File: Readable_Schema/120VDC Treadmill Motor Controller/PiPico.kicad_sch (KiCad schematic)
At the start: 1 part

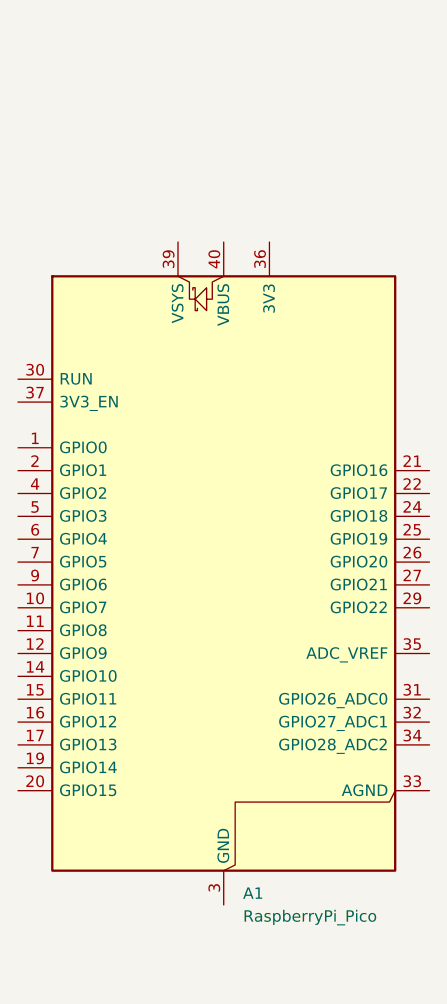
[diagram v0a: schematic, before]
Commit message: I cant for the life of me get the current sensing to actually properly scale with current, I treid 5 different sim models and right now the DA is the best but doesnt start showing anything till around 19amps which kind of defeats the purpose
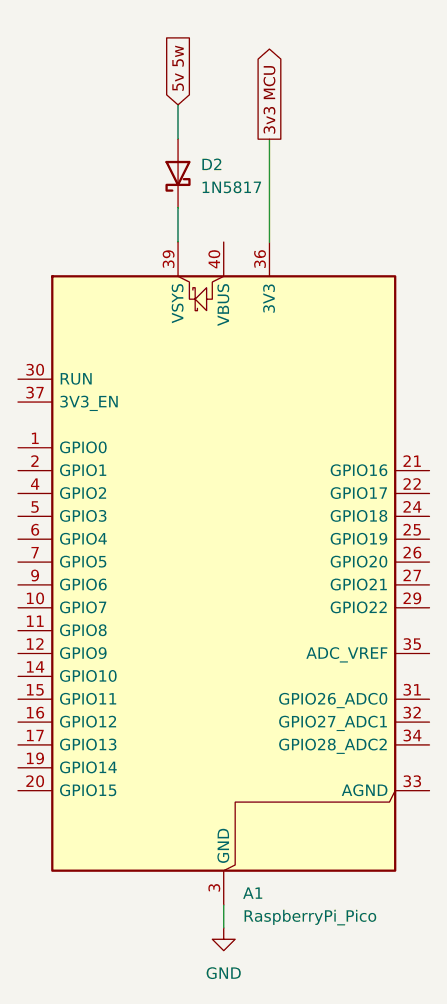
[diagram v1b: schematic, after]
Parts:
- added D2: 1N5817, Diode_THT:D_DO-41_SOD81_P10.16mm_Horizontal, symbol Diode:1N5817
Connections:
- net GND: now reaches A1.13 (GND), A1.18 (GND), A1.23 (GND), A1.28 (GND), A1.3 (GND), A1.38 (GND), A1.8 (GND)
- net 3v3 MCU: now reaches A1.36 (3V3)
- net at A1.39 (VSYS): now also D2.1 (K)
- new net 5v 5w: D2.2 (A)
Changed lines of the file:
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@@
 	(generator_version "9.0")
 	(paper "A4")
+	(wire
+		(pts
+			(xy 135.89 58.42) (xy 135.89 62.23)
+		)
+		(stroke
+			(width 0)
+			(type default)
+		)
+	)
+	(wire
+		(pts
+			(xy 135.89 46.99) (xy 135.89 50.8)
+		)
+		(stroke
+			(width 0)
+			(type default)
+		)
+	)
+	(wire
+		(pts
+			(xy 140.97 135.89) (xy 140.97 138.43)
+		)
+		(stroke
+			(width 0)
+			(type default)
+		)
+	)
+	(wire
+		(pts
+			(xy 146.05 50.8) (xy 146.05 62.23)
+		)
+		(stroke
+			(width 0)
+			(type default)
+		)
+	)
+	(global_label "5v 5w"
+		(shape input)
+		(at 135.89 46.99 90)
+		(fields_autoplaced yes)
+		(effects
+			(font
+				(size 1.27 1.27)
+			)
+			(justify left)
+		)
+		(property "Intersheetrefs" "${INTERSHEET_REFS}"
+			(at 135.89 38.3201 90)
+			(effects
+				(font
+					(size 1.27 1.27)
+				)
+				(justify left)
+				(hide yes)
+			)
+		)
+	)
+	(global_label "3v3 MCU"
+		(shape output)
+		(at 146.05 50.8 90)
+		(fields_autoplaced yes)
+		(effects
+			(font
+				(size 1.27 1.27)
+			)
+			(justify left)
+		)
+		(property "Intersheetrefs" "${INTERSHEET_REFS}"
+			(at 146.05 39.4087 90)
+			(effects
+				(font
+					(size 1.27 1.27)
+				)
+				(justify left)
+				(hide yes)
+			)
+		)
+	)
 	(symbol
 		(lib_id "MCU_Module:RaspberryPi_Pico")
@@
 					(unit 1)
 				)
+			)
+		)
+	)
+	(symbol
+		(lib_id "power:GND")
+		(at 140.97 138.43 0)
+		(unit 1)
+		(exclude_from_sim no)
+		(in_bom yes)
+		(on_board yes)
+		(dnp no)
+		(fields_autoplaced yes)
+		(property "Reference" "#PWR03"
+			(at 140.97 144.78 0)
+			(effects
+				(font
+					(size 1.27 1.27)
+				)
+				(hide yes)
+			)
+		)
+		(property "Value" "GND"
+			(at 140.97 143.51 0)
+			(effects
+				(font
+					(size 1.27 1.27)
+				)
+			)
+		)
+		(property "Footprint" ""
+			(at 140.97 138.43 0)
+			(effects
+				(font
+					(size 1.27 1.27)
+				)
+				(hide yes)
+			)
+		)
+		(property "Datasheet" ""
+			(at 140.97 138.43 0)
+			(effects
+				(font
+					(size 1.27 1.27)
+				)
+				(hide yes)
+			)
+		)
+		(property "Description" "Power symbol creates a global label with name \"GND\" , ground"
+			(at 140.97 138.43 0)
+			(effects
+				(font
+					(size 1.27 1.27)
+				)
+				(hide yes)
+			)
+		)
+		(pin "1"
+		)
+		(instances
+			(project ""
+				(path "/319bc5c0-2dd5-4df3-a34b-9170833ebccd/dc45a2ff-df18-49a4-81ff-80d10381c9e9"
+					(reference "#PWR03")
+					(unit 1)
+				)
+			)
+		)
+	)
+	(symbol
+		(lib_id "Diode:1N5817")
+		(at 135.89 54.61 90)
+		(unit 1)
+		(exclude_from_sim no)
+		(in_bom yes)
+		(on_board yes)
+		(dnp no)
+		(fields_autoplaced yes)
+		(property "Reference" "D2"
+			(at 138.43 53.6574 90)
+			(effects
+				(font
+					(size 1.27 1.27)
+				)
+				(justify right)
+			)
+		)
+		(property "Value" "1N5817"
+			(at 138.43 56.1974 90)
+			(effects
+				(font
+					(size 1.27 1.27)
+				)
+				(justify right)
+			)
+		)
+		(property "Footprint" "Diode_THT:D_DO-41_SOD81_P10.16mm_Horizontal"
+			(at 140.335 54.61 0)
+			(effects
+				(font
+					(size 1.27 1.27)
+				)
+				(hide yes)
+			)
+		)
+		(property "Datasheet" "http://www.vishay.com/docs/88525/1n5817.pdf"
+			(at 135.89 54.61 0)
+			(effects
+				(font
+					(size 1.27 1.27)
+				)
+				(hide yes)
+			)
+		)
+		(property "Description" "20V 1A Schottky Barrier Rectifier Diode, DO-41"
+			(at 135.89 54.61 0)
+			(effects
+				(font
+					(size 1.27 1.27)
+				)
+				(hide yes)
+			)
+		)
+		(pin "1"
+		)
+		(pin "2"
+		)
+		(instances
+			(project ""
+				(path "/319bc5c0-2dd5-4df3-a34b-9170833ebccd/dc45a2ff-df18-49a4-81ff-80d10381c9e9"
+					(reference "D2")
+					(unit 1)
+				)

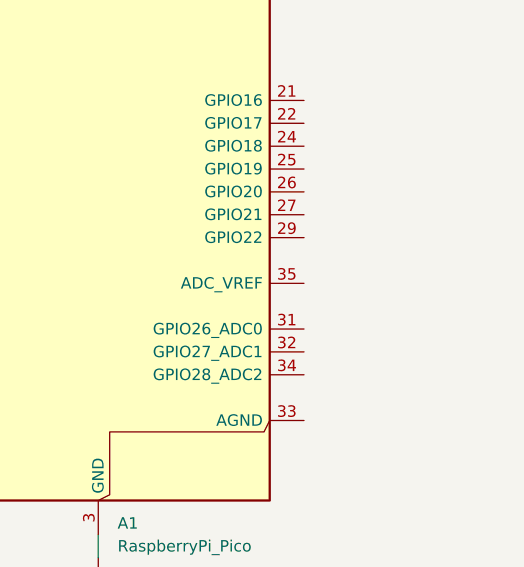
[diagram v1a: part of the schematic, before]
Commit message: Continuing to update footprints, did some follow up math on low pass filter for adc voltage coming out of current sense system
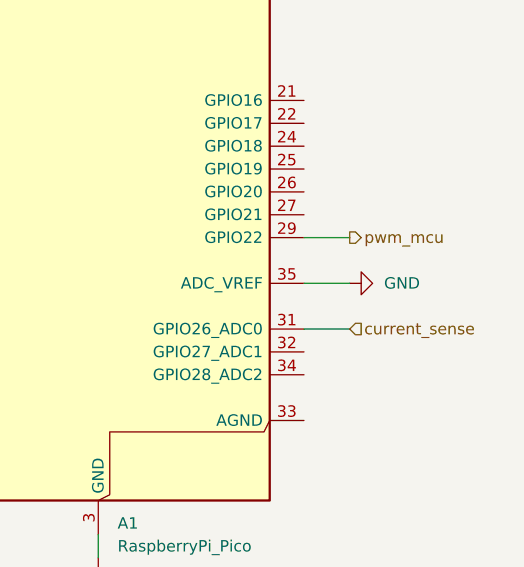
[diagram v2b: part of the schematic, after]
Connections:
- net GND: now also A1.35 (ADC_VREF)
- net pwm_mcu: now reaches A1.29 (GPIO22)
- net current_sense: now reaches A1.31 (GPIO26_ADC0)
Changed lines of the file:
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@@
+	(wire
+		(pts
+			(xy 163.83 107.95) (xy 168.91 107.95)
+		)
+		(stroke
+			(width 0)
+			(type default)
+		)
+	)
 	(wire
 		(pts
@@
 	(wire
 		(pts
+			(xy 163.83 102.87) (xy 168.91 102.87)
+		)
+		(stroke
+			(width 0)
+			(type default)
+		)
+	)
+	(wire
+		(pts
 			(xy 140.97 135.89) (xy 140.97 138.43)
 		)
@@
 		(pts
 			(xy 146.05 50.8) (xy 146.05 62.23)
+		)
+		(stroke
+			(width 0)
+			(type default)
+		)
+	)
+	(wire
+		(pts
+			(xy 163.83 113.03) (xy 168.91 113.03)
 		)
 		(stroke
@@
 				(hide yes)
 			)
+		)
+	)
+	(hierarchical_label "pwm_mcu"
+		(shape output)
+		(at 168.91 102.87 0)
+		(effects
+			(font
+				(size 1.27 1.27)
+			)
+			(justify left)
+		)
+	)
+	(hierarchical_label "current_sense"
+		(shape input)
+		(at 168.91 113.03 0)
+		(effects
+			(font
+				(size 1.27 1.27)
+			)
+			(justify left)
 		)
 	)
@@
 					(unit 1)
 				)
+			)
+		)
+	)
+	(symbol
+		(lib_id "power:GND")
+		(at 168.91 107.95 90)
+		(unit 1)
+		(exclude_from_sim no)
+		(in_bom yes)
+		(on_board yes)
+		(dnp no)
+		(fields_autoplaced yes)
+		(property "Reference" "#PWR020"
+			(at 175.26 107.95 0)
+			(effects
+				(font
+					(size 1.27 1.27)
+				)
+				(hide yes)
+			)
+		)
+		(property "Value" "GND"
+			(at 172.72 107.9499 90)
+			(effects
+				(font
+					(size 1.27 1.27)
+				)
+				(justify right)
+			)
+		)
+		(property "Footprint" ""
+			(at 168.91 107.95 0)
+			(effects
+				(font
+					(size 1.27 1.27)
+				)
+				(hide yes)
+			)
+		)
+		(property "Datasheet" ""
+			(at 168.91 107.95 0)
+			(effects
+				(font
+					(size 1.27 1.27)
+				)
+				(hide yes)
+			)
+		)
+		(property "Description" "Power symbol creates a global label with name \"GND\" , ground"
+			(at 168.91 107.95 0)
+			(effects
+				(font
+					(size 1.27 1.27)
+				)
+				(hide yes)
+			)
+		)
+		(pin "1"
+		)
+		(instances
+			(project "120VDC Treadmill Motor Controller"
+				(path "/319bc5c0-2dd5-4df3-a34b-9170833ebccd/dc45a2ff-df18-49a4-81ff-80d10381c9e9"
+					(reference "#PWR020")
+					(unit 1)
+				)

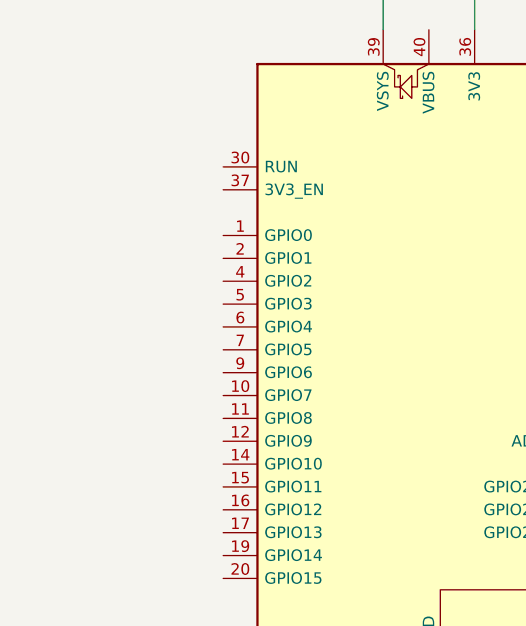
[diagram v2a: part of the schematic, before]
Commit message: continued to add footprints, we still need to add hall effect circuit and possible brake resistor subcircuit. We may also want to consider switching the large 15v isolated power supplies to be smd as well as the FOD3182. Otherwise this will become a lot to hand solder.
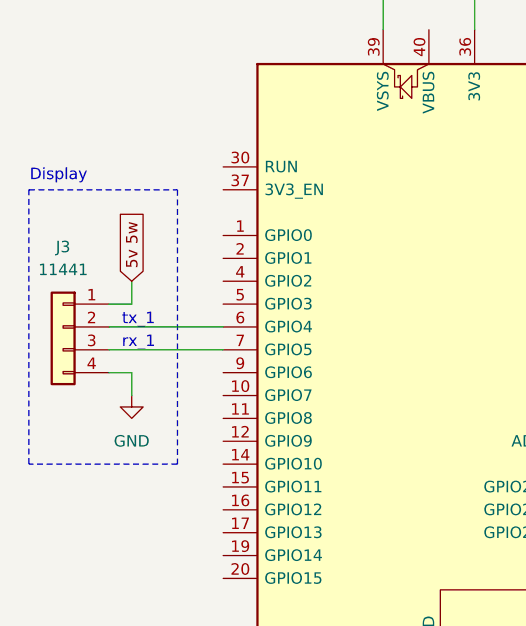
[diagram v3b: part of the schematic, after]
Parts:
- added J3: 11441, Connector_PinHeader_2.54mm:PinHeader_1x04_P2.54mm_Vertical, symbol Connector_Generic:Conn_01x04
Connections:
- net 5v 5w: now also J3.1 (Pin_1)
- net GND: now also J3.4 (Pin_4)
- net at A1.6 (GPIO4): now also J3.2 (Pin_2)
- net at A1.7 (GPIO5): now also J3.3 (Pin_3)
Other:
- note added: "Display"
- note added: "rx_1"
- note added: "tx_1"

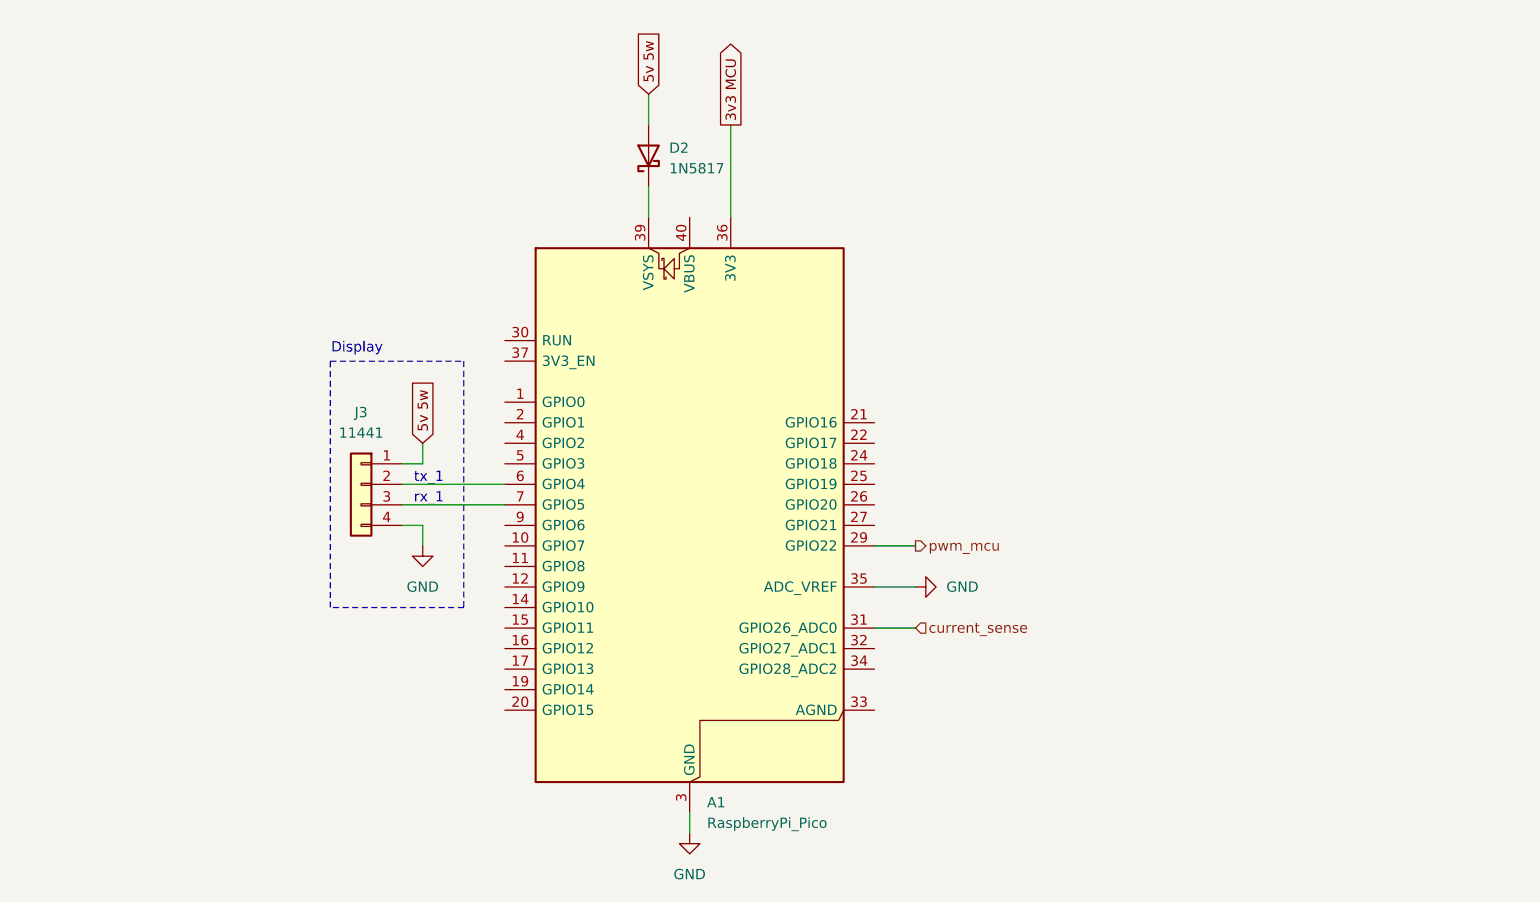
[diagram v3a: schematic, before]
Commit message: -There are no power supply/ gate driver variants for the ones chosen that support smd -We NEED to workout how we want to communicate with both linuxCNC for the CNC controller and a potentiometer for the bridgeport -We NEED to incorporate a ESTOP component that directly shuts off the motor -Missing brake resistor subcircuit -Missing Input capacitors to deal with back EMF
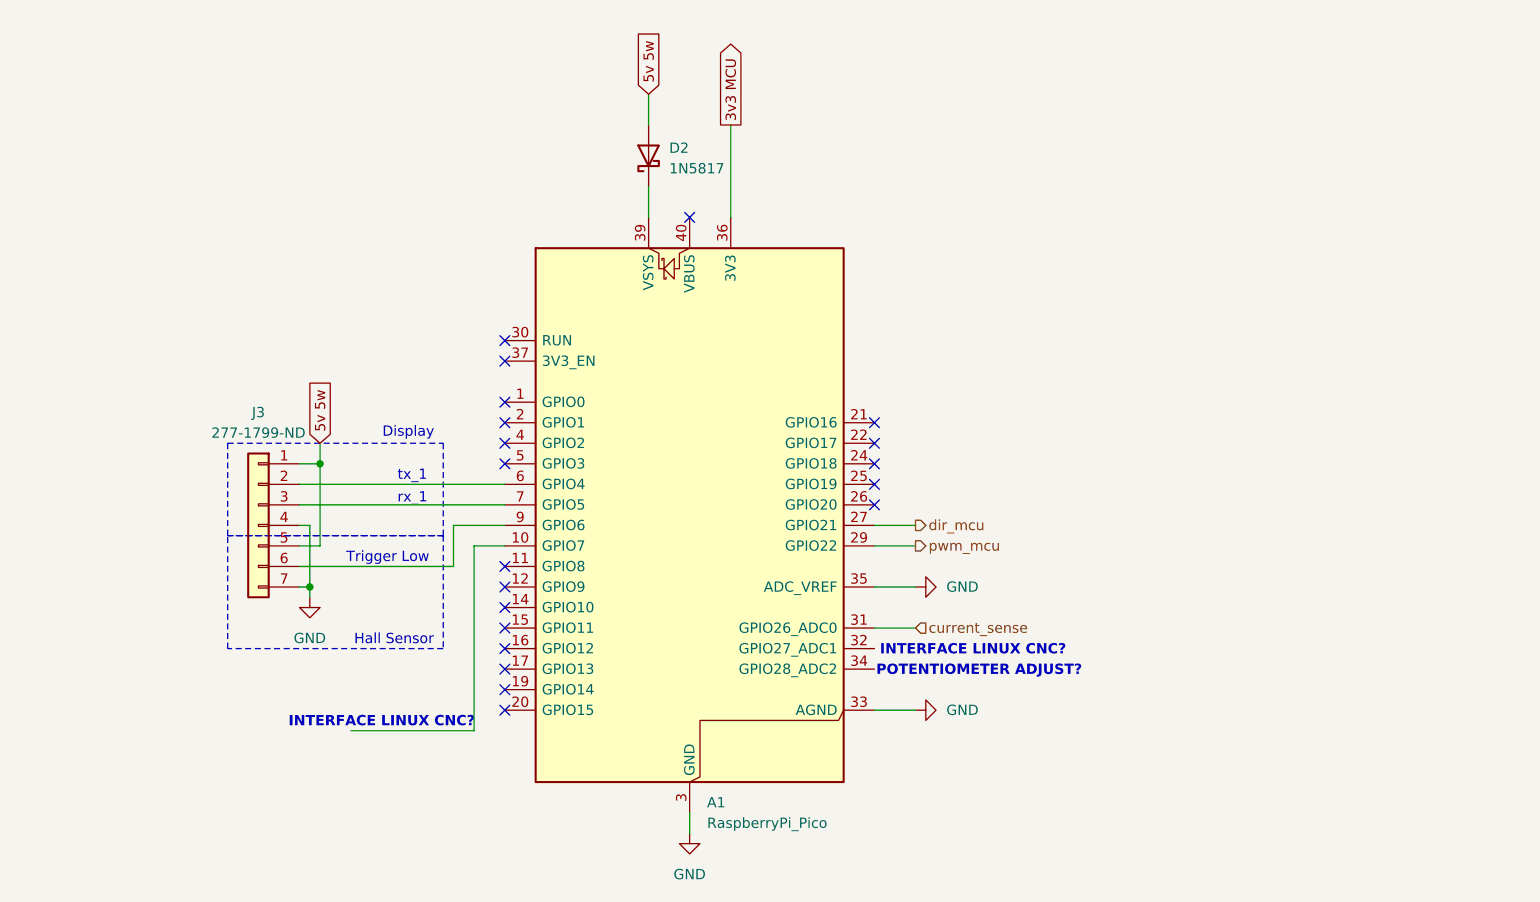
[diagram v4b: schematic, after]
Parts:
- removed J3: 11441, Connector_PinHeader_2.54mm:PinHeader_1x04_P2.54mm_Vertical, symbol Connector_Generic:Conn_01x04
- added J3: 277-1799-ND, Treadmill_Feet:PHOENIX_1990054, symbol Connector_Generic:Conn_01x07
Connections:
- net 5v 5w: now also J3.1 (Pin_1), J3.5 (Pin_5)
- net GND: now also A1.33 (AGND), J3.4 (Pin_4), J3.7 (Pin_7)
- net dir_mcu: now reaches A1.27 (GPIO21)
- net at A1.6 (GPIO4): now also J3.2 (Pin_2)
- net at A1.7 (GPIO5): now also J3.3 (Pin_3)
- net at A1.9 (GPIO6): now also J3.6 (Pin_6)
- no-connect marks 0 -> 20
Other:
- note added: "Hall Sensor"
- note added: "INTERFACE LINUX CNC?"
- note added: "POTENTIOMETER ADJUST?"
- note added: "Trigger Low"

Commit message: Still need to do the majority of the things mentioned in the last commit, made some progress on the mcu pinout headers, fixed a few resistors that were putting npns in a high side drive state (preventing fully grounding signal)
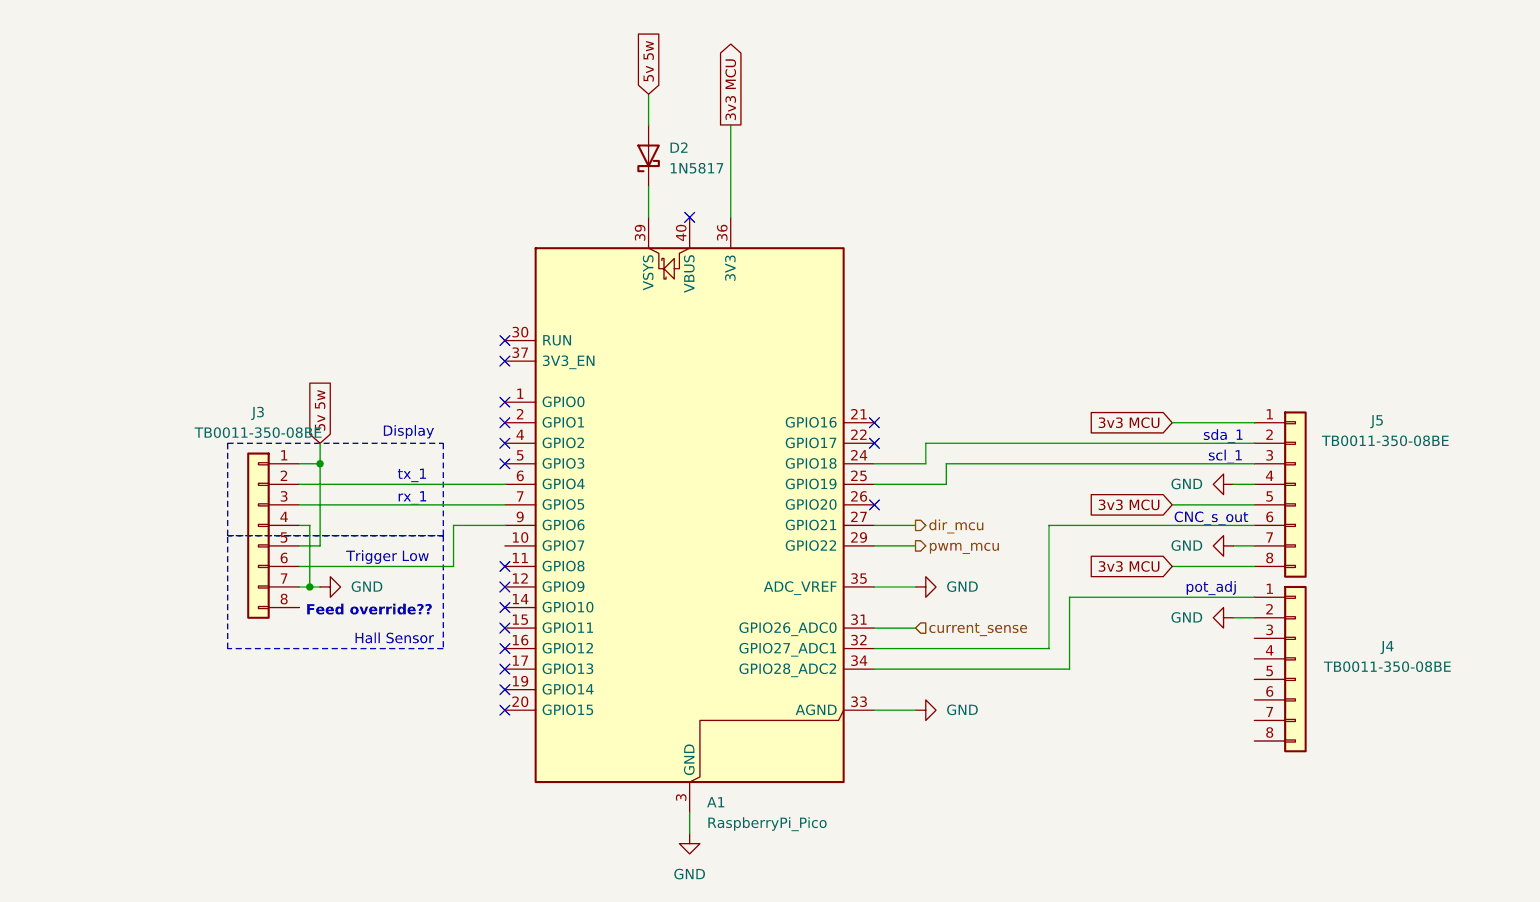
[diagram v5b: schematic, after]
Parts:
- removed J3: 277-1799-ND, Treadmill_Feet:PHOENIX_1990054, symbol Connector_Generic:Conn_01x07
- added J3, J4, J5: TB0011-350-08BE, Connector_Wago:Wago_734-138_1x08_P3.50mm_Vertical, symbol Connector_Generic:Conn_01x08
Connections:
- net 3v3 MCU: now also J5.1 (Pin_1), J5.5 (Pin_5), J5.8 (Pin_8)
- net 5v 5w: now also J3.1 (Pin_1), J3.5 (Pin_5)
- net GND: now also J3.4 (Pin_4), J3.7 (Pin_7), J4.2 (Pin_2), J5.4 (Pin_4), J5.7 (Pin_7)
- net at A1.24 (GPIO18): now also J5.2 (Pin_2)
- net at A1.25 (GPIO19): now also J5.3 (Pin_3)
- net at A1.32 (GPIO27_ADC1): now also J5.6 (Pin_6)
- net at A1.34 (GPIO28_ADC2): now also J4.1 (Pin_1)
- net at A1.6 (GPIO4): now also J3.2 (Pin_2)
- net at A1.7 (GPIO5): now also J3.3 (Pin_3)
- net at A1.9 (GPIO6): now also J3.6 (Pin_6)
- no-connect marks 20 -> 18
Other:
- note added: "CNC_s_out"
- note added: "Feed override??"
- note added: "pot_adj"
- note added: "scl_1"
- note added: "sda_1"
- note removed: "INTERFACE LINUX CNC?"
- note removed: "POTENTIOMETER ADJUST?"
